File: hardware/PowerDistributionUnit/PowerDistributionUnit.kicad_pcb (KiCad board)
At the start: 2 copper layers, 99.1 x 62.2 mm, 95 parts, among them J1 973582101, J2 973582100, J3 973582101, J4 973582100, Q1 SQJ141ELP, Q2 CSD18511Q5A, SW1 SW_Push, U1 TPS25983, U2 AD5258, U3 NUCLEO_L432KC

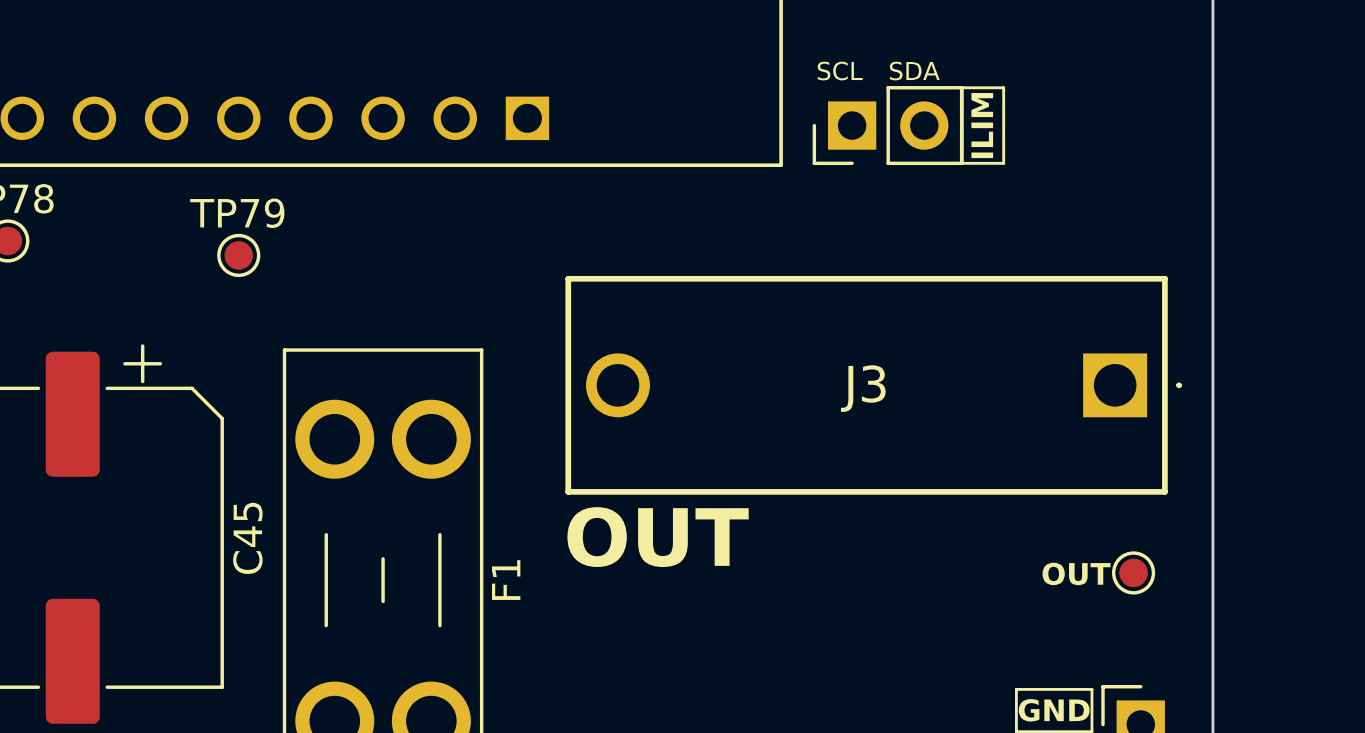
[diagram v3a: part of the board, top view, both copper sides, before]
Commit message: added net classes, added out test point (prev. only efuse_out)
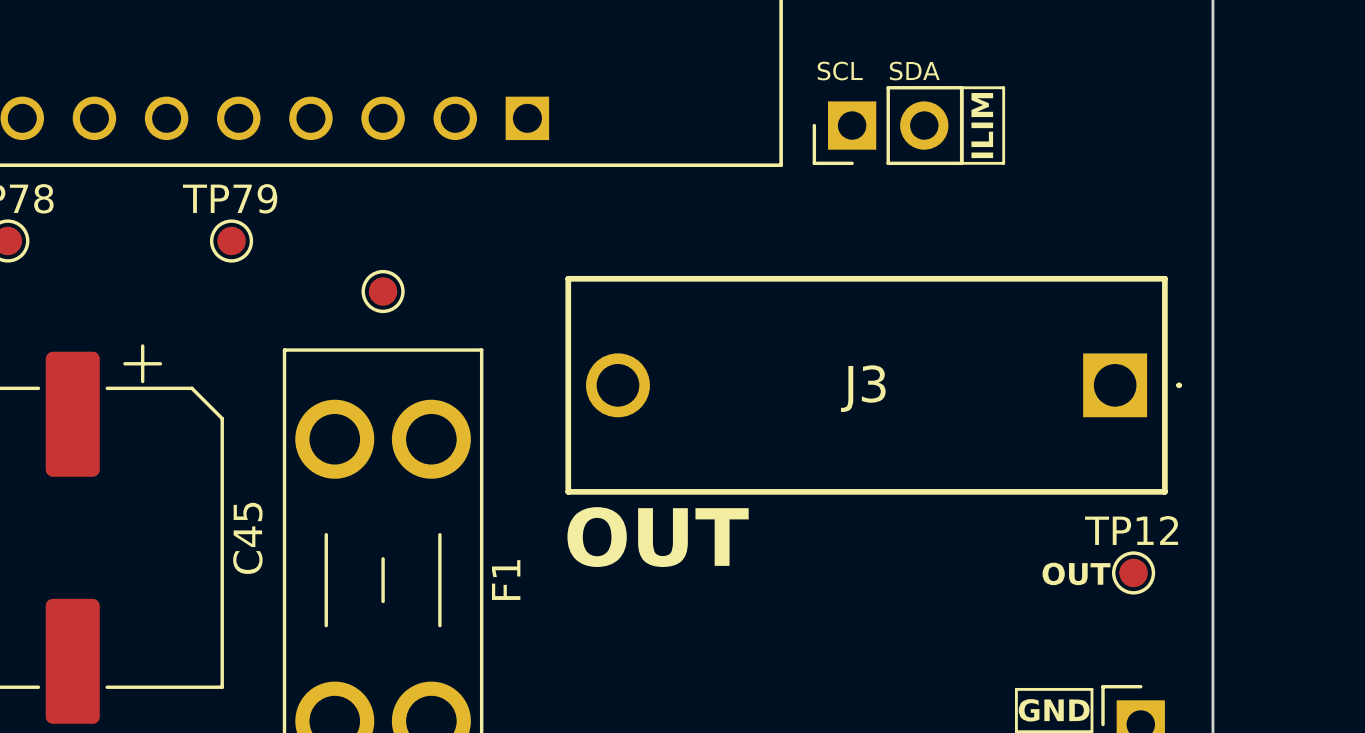
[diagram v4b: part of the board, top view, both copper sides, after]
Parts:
- added TP12: VOUT, TestPoint:TestPoint_Pad_D1.0mm, F.Cu at (157.7, 126.7)
- JP77: value OVLO_DISABLE -> OVLO_ENABLE
- TP86: value VOUT -> EFUSE_OUT
- moved TP86 28.2 mm to (131.3, 116.8)
- moved TP79 0.57 mm to (126.0, 115.1)
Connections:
- net Net-(J3-Pin_1) renamed /OUT
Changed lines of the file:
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@@
 	(net 23 "/IN")
 	(net 24 "Net-(D3-A)")
-	(net 25 "Net-(J3-Pin_1)")
+	(net 25 "/OUT")
 	(net 26 "/ILIM")
 	(net 27 "Net-(JP1-A)")
@@
 		(tags "Through hole pin header THT 1x02 2.54mm single row")
 		(property "Reference" "JP2"
-			(at 0 -2.33 360)
+			(at 0 -2.33 0)
 			(layer "F.SilkS")
 			(hide yes)
@@
 		)
 		(property "Value" "Jumper_2_Small_Open"
-			(at 0 4.87 360)
+			(at 0 4.87 0)
 			(layer "F.Fab")
 			(effects
@@
 	(footprint "TestPoint:TestPoint_Pad_D1.0mm"
 		(layer "F.Cu")
-		(at 157.734 126.746)
+		(at 131.318 116.84)
 		(descr "SMD pad as test Point, diameter 1.0mm")
 		(tags "test point SMD pad")
@@
 			)
 		)
-		(property "Value" "VOUT"
+		(property "Value" "EFUSE_OUT"
 			(at 0 1.55 0)
 			(layer "F.Fab")
@@
 	(footprint "TestPoint:TestPoint_Pad_D1.0mm"
 		(layer "F.Cu")
-		(at 126.238 115.57)
+		(at 125.984 115.062)
 		(descr "SMD pad as test Point, diameter 1.0mm")
 		(tags "test point SMD pad")
@@
 		)
 		(property "Value" "PG"
-			(at 0 1.55 0)
+			(at 8.128 1.296 0)
 			(layer "F.Fab")
 			(effects
@@
 		)
 		(fp_text user "${REFERENCE}"
-			(at 0 1.27 360)
+			(at 0 1.27 0)
 			(layer "F.Fab")
 			(effects
@@
 		(tags "resistor")
 		(property "Reference" "R59"
-			(at 5.634 0.366 -0)
+			(at 5.634 0.366 0)
 			(layer "B.SilkS")
 			(effects
@@
 		)
 		(property "Value" "102k"
-			(at 0 1.65 360)
+			(at 0 1.65 0)
 			(layer "F.Fab")
 			(effects
@@
 		)
 		(fp_text user "${REFERENCE}"
-			(at 0 0 360)
+			(at 0 0 0)
 			(layer "F.Fab")
 			(effects
@@
 		)
 		(property "Value" "100k"
-			(at 0 1.65 360)
+			(at 0 1.65 0)
 			(layer "F.Fab")
 			(effects
@@
 		)
 		(fp_text user "${REFERENCE}"
-			(at 0 0 360)
+			(at 0 0 0)
 			(layer "F.Fab")
 			(effects
@@
 			(layers "*.Cu" "*.Mask")
 			(remove_unused_layers no)
-			(net 25 "Net-(J3-Pin_1)")
+			(net 25 "/OUT")
 			(pinfunction "Pin_1")
 			(pintype "passive")
@@
 			(layers "*.Cu" "*.Mask")
 			(remove_unused_layers no)
-			(net 25 "Net-(J3-Pin_1)")
+			(net 25 "/OUT")
 			(pinfunction "Pin_1")
 			(pintype "passive")
@@
 			(layers "*.Cu" "*.Mask")
 			(remove_unused_layers no)
-			(net 25 "Net-(J3-Pin_1)")
+			(net 25 "/OUT")
 			(pintype "passive")
 		)
@@
 			(layers "*.Cu" "*.Mask")
 			(remove_unused_layers no)
-			(net 25 "Net-(J3-Pin_1)")
+			(net 25 "/OUT")
 			(pintype "passive")
 		)
@@
 		)
 	)
+	(footprint "TestPoint:TestPoint_Pad_D1.0mm"
+		(layer "F.Cu")
+		(at 157.734 126.746)
+		(descr "SMD pad as test Point, diameter 1.0mm")
+		(tags "test point SMD pad")
+		(property "Reference" "TP12"
+			(at 0 -1.448 0)
+			(layer "F.SilkS")
+			(effects
+				(font
+					(size 1 1)
+					(thickness 0.15)
+				)
+			)
+		)
+		(property "Value" "VOUT"
+			(at 0 1.55 0)
+			(layer "F.Fab")
+			(effects
+				(font
+					(size 1 1)
+					(thickness 0.15)
+				)
+			)
+		)
+		(property "Footprint" "TestPoint:TestPoint_Pad_D1.0mm"
+			(at 0 0 0)
+			(unlocked yes)
+			(layer "F.Fab")
+			(hide yes)
+			(effects
+				(font
+					(size 1.27 1.27)
+					(thickness 0.15)
+				)
+			)
+		)
+		(property "Datasheet" ""
+			(at 0 0 0)
+			(unlocked yes)
+			(layer "F.Fab")
+			(hide yes)
+			(effects
+				(font
+					(size 1.27 1.27)
+					(thickness 0.15)
+				)
+			)
+		)
+		(property "Description" "test point"
+			(at 0 0 0)
+			(unlocked yes)
+			(layer "F.Fab")
+			(hide yes)
+			(effects
+				(font
+					(size 1.27 1.27)
+					(thickness 0.15)
+				)
+			)
+		)
+		(property ki_fp_filters "Pin* Test*")
+		(sheetname "Root")
+		(sheetfile "PowerDistributionUnit.kicad_sch")
+		(attr exclude_from_pos_files)
+		(fp_circle
+			(center 0 0)
+			(end 0 0.7)
+			(stroke
+				(width 0.12)
+				(type solid)
+			)
+			(fill none)
+			(layer "F.SilkS")
+		)
+		(fp_circle
+			(center 0 0)
+			(end 1 0)
+			(stroke
+				(width 0.05)
+				(type solid)
+			)
+			(fill none)
+			(layer "F.CrtYd")
+		)
+		(fp_text user "${REFERENCE}"
+			(at 0 -1.45 0)
+			(layer "F.Fab")
+			(effects
+				(font
+					(size 1 1)
+					(thickness 0.15)
+				)
+			)
+		)
+		(pad "1" smd circle
+			(at 0 0)
+			(size 1 1)
+			(layers "F.Cu" "F.Mask")
+			(net 25 "/OUT")
+			(pinfunction "1")
+			(pintype "passive")
+		)
+	)
 	(footprint "Capacitor_SMD:C_0805_2012Metric"
 		(layer "F.Cu")
@@
 		)
 		(property "Value" "ILIM"
-			(at 22.699 3.566 -0)
+			(at 22.699 3.566 0)
 			(layer "B.Fab")
 			(effects
@@
 		)
 		(fp_text user "${REFERENCE}"
-			(at 22.699 0.566 -0)
+			(at 22.699 0.566 0)
 			(layer "B.Fab")
 			(effects
@@
 		)
 		(fp_text user "${REFERENCE}"
-			(at 0 1.27 360)
+			(at 0 1.27 0)
 			(layer "F.Fab")
 			(effects
@@
 		)
 		(property "Value" "972k"
-			(at 0 1.65 360)
+			(at 0 1.65 0)
 			(layer "F.Fab")
 			(effects
@@
 		)
 		(fp_text user "${REFERENCE}"
-			(at 0 0 360)
+			(at 0 0 0)
 			(layer "F.Fab")
 			(effects
@@
 			)
 		)
-		(property "Value" "OVLO_DISABLE"
+		(property "Value" "OVLO_ENABLE"
 			(at 0 4.87 90)
 			(layer "F.Fab")
@@
 		)
 		(fp_text user "${REFERENCE}"
-			(at 0 1.27 360)
+			(at 0 1.27 0)
 			(layer "F.Fab")
 			(effects
@@
 		)
 		(fp_text user "${REFERENCE}"
-			(at 0 1.27 360)
+			(at 0 1.27 0)
 			(layer "F.Fab")
 			(effects
@@
 		(tags "resistor")
 		(property "Reference" "R50"
-			(at 0 -1.65 360)
+			(at 0 -1.65 0)
 			(layer "F.SilkS")
 			(effects
@@
 		)
 		(property "Value" "1.13"
-			(at 0 1.65 360)
+			(at 0 1.65 0)
 			(layer "F.Fab")
 			(effects
@@
 		)
 		(fp_text user "${REFERENCE}"
-			(at 0 0 360)
+			(at 0 0 0)
 			(layer "F.Fab")
 			(effects

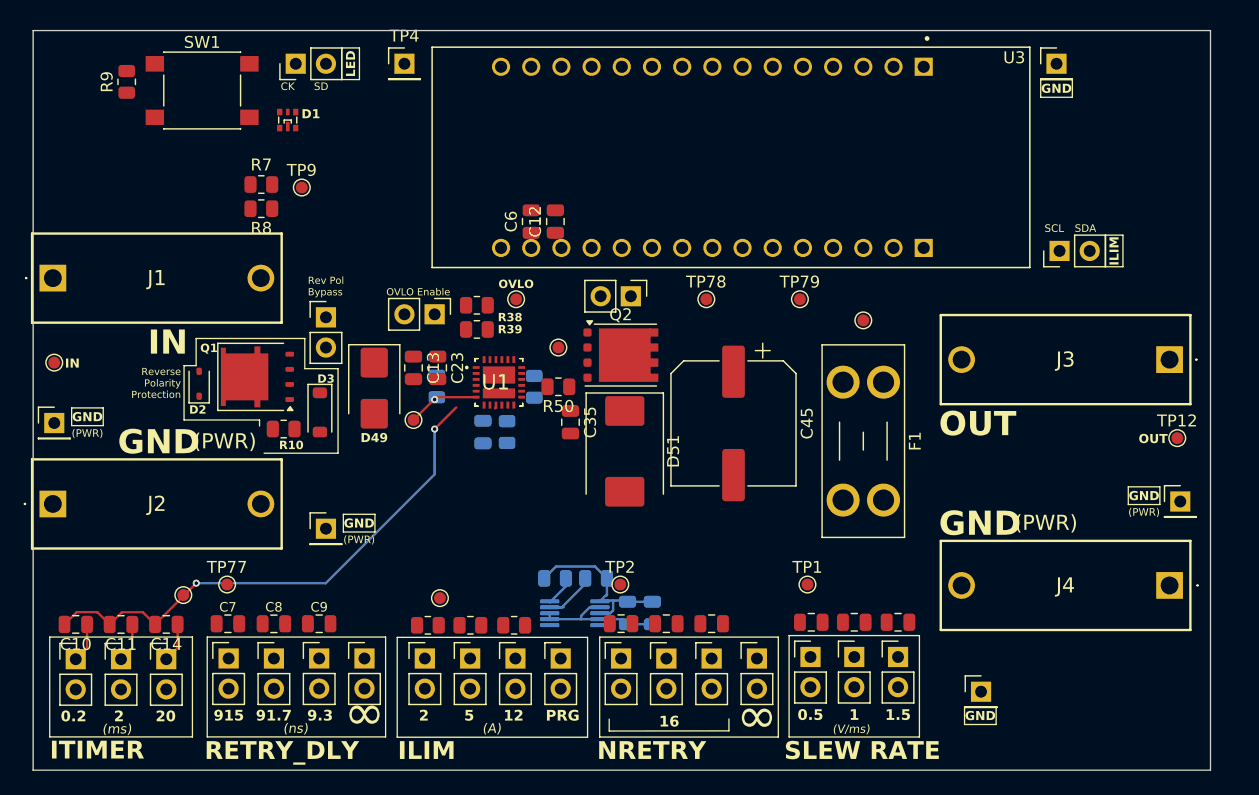
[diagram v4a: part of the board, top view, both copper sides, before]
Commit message: added mounting holes
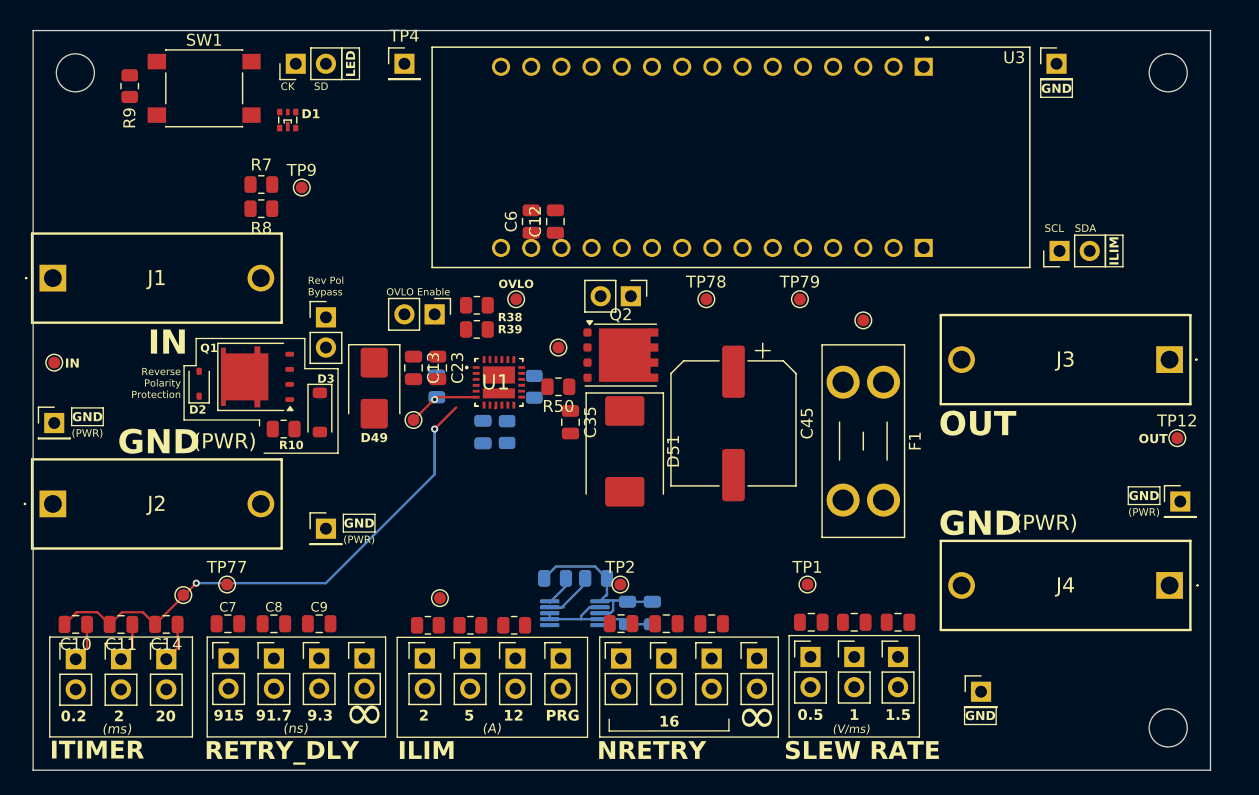
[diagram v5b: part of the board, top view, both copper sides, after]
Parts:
- added H1: MountingHole, MountingHole:MountingHole_3.2mm_M3, F.Cu at (65.0, 96.0)
- added H2: MountingHole, MountingHole:MountingHole_3.2mm_M3, F.Cu at (157.0, 96.0)
- added H3: MountingHole, MountingHole:MountingHole_3.2mm_M3, F.Cu at (157.0, 151.1)
- moved R9 0.44 mm to (69.6, 97.1)
- moved SW1 0.25 mm to (75.9, 97.3)

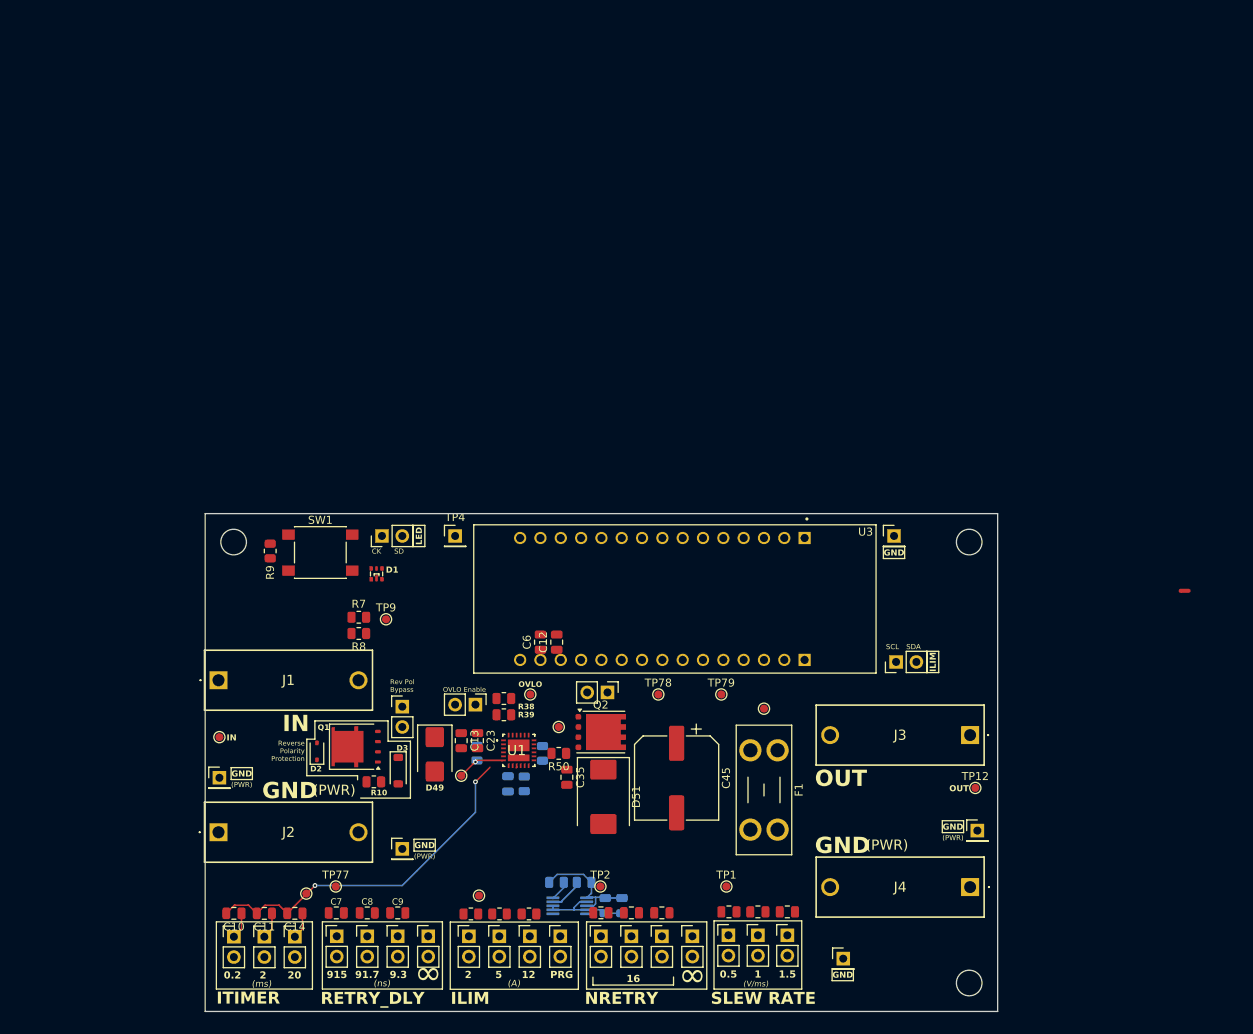
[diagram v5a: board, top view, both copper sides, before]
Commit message: added pours, traces, & labels, revised courtyard around TPS25983 footprint, added another net tie, ...
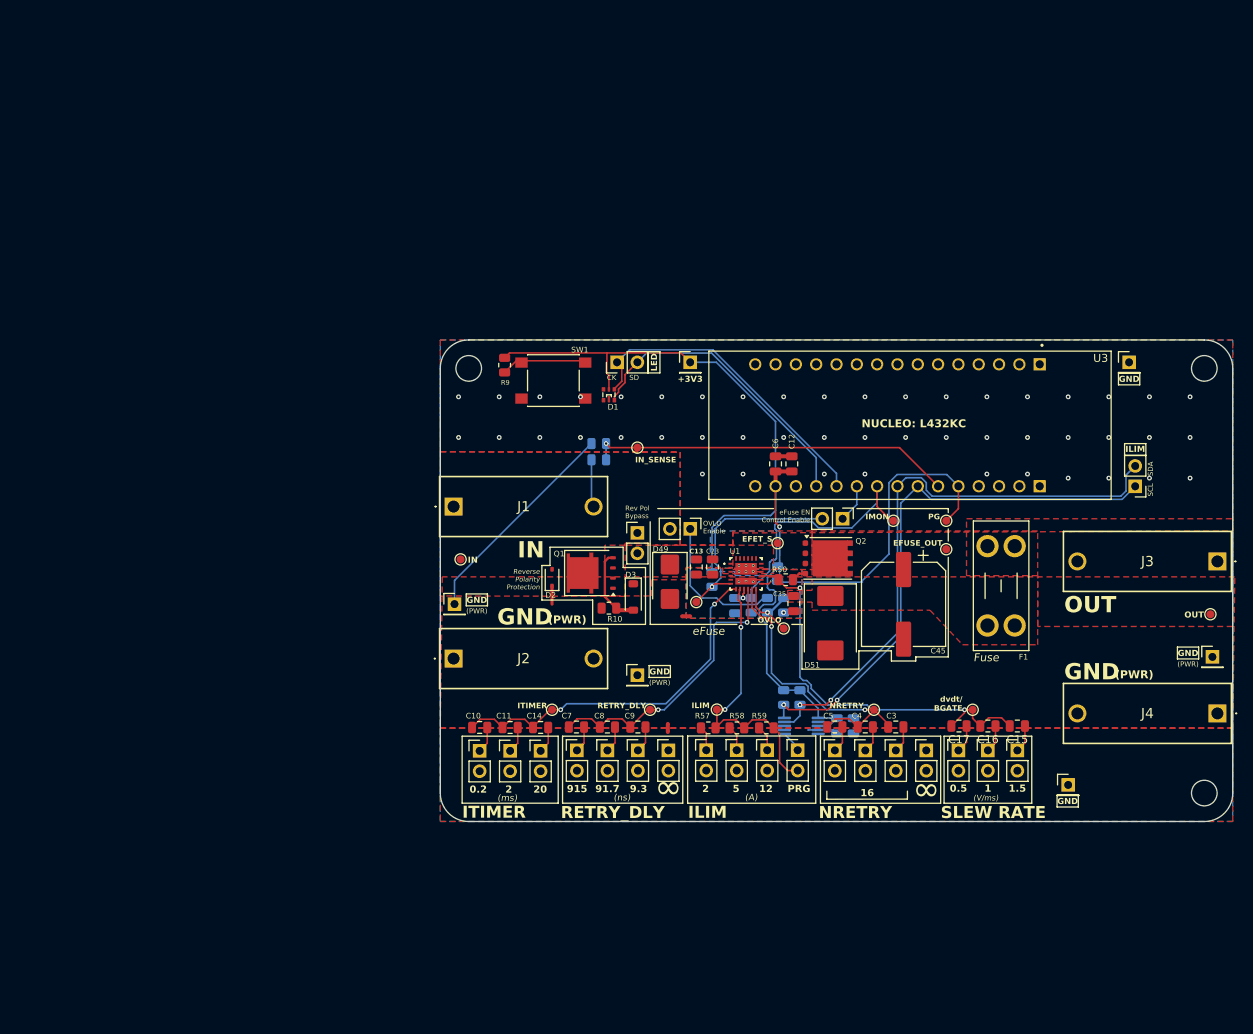
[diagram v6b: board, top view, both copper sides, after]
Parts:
- added NT2: NetTie_2, NetTie:NetTie-2_SMD_Pad0.5mm, F.Cu at (121.6, 105.3)
- R38, R39, R7, R8: moved to B.Cu
- moved NT1 66.8 mm to (119.3, 119.3), turned to -90 degrees
- moved TP77 45.1 mm to (117.1, 117.0)
- moved TP2 40.7 mm to (145.1, 117.0)
- moved JP12 38.5 mm to (99.6, 122.1)
- moved JP13 38.5 mm to (103.4, 122.1)
- moved C11 38.5 mm to (99.6, 119.2)
- moved C14 38.5 mm to (103.4, 119.2)
- moved JP11 38.5 mm to (95.8, 122.1)
- moved C10 38.5 mm to (95.8, 119.2)
- moved TP3 38.4 mm to (104.8, 117.0)
- moved R8 38.3 mm to (110.7, 83.7)
- moved TP9 38.0 mm to (115.5, 84.2)
- moved C8 38.0 mm to (111.7, 119.1)
- moved JP8 38.0 mm to (111.7, 122.1)
- moved C7 38.0 mm to (107.9, 119.1)
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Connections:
- U3 pad CN4_11: /LED_SD -> /LED_CK
- U3 pad CN4_12: /LED_CK -> /LED_SD
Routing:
- net +3V3: track 15.0 -> 115.1 mm, vias 0 -> 1
- net /ILIM_SDA: track 5.43 -> 72.6 mm, vias 0 -> 2
- net /ILIM_SCL: track 2.60 -> 68.6 mm, vias 0 -> 2
- net /dVdt/BGATE: track 0.00 -> 49.8 mm, vias 0 -> 2
- net /IN_SENSE: track 0.00 -> 45.7 mm, vias 0 -> 1
- net /PG: track 0.00 -> 41.4 mm, vias 0 -> 1
- net /LED_CK: track 0.00 -> 40.1 mm
- net /LED_SD: track 0.00 -> 37.7 mm
- net /NRETRY: track 0.00 -> 37.5 mm, vias 0 -> 2
- net /RETRY_DLY: track 0.00 -> 36.3 mm, vias 0 -> 2
- net /ILIM: track 0.00 -> 35.9 mm, vias 0 -> 2
- net /IMON: track 0.17 -> 35.9 mm, vias 0 -> 1
- net GNDPWR: track 0.00 -> 29.4 mm
- net /EN_PIN: track 5.87 -> 27.1 mm
- net Net-(JP77-A): track 0.00 -> 18.1 mm
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- added copper zone on F.Cu, net /EFET_S
- added copper zone on B.Cu, net /EFUSE_IN
- added copper zone on F.Cu, net /EFUSE_IN
- added copper zone on F.Cu, net /EFUSE_OUT
- added copper zone on F.Cu, net /IN
- added copper zone on F.Cu, net /OUT
- added copper zone on B.Cu, net GND
- added copper zone on F.Cu, net GND
- added copper zone on F.Cu, net GNDPWR
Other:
- board size 99.1 x 62.2 mm -> 99.1 x 60.2 mm
- board text added: "+3V3"
- board text added: "EFET_S"
- board text added: "EFUSE_OUT"
- board text added: "Fuse"
- board text added: "IMON"
- board text added: "IN_SENSE"
- board text added: "NUCLEO: L432KC"
- board text added: "PG"
- board text added: "dvdt/ BGATE"
- board text added: "eFuse"
- board text added: "eFuse EN Control Enable"
